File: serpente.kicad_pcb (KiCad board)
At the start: 2 copper layers, 24 x 22 mm, 31 parts, among them J1 USB_C_Receptacle_USB2.0, J2 Conn_Power, J3 Conn_GPIO, SW1 SW_RESET, U1 GD25Q32CNIGR, U2 MCP1700-3302E_SOT23, U3 ATSAMD21E18A

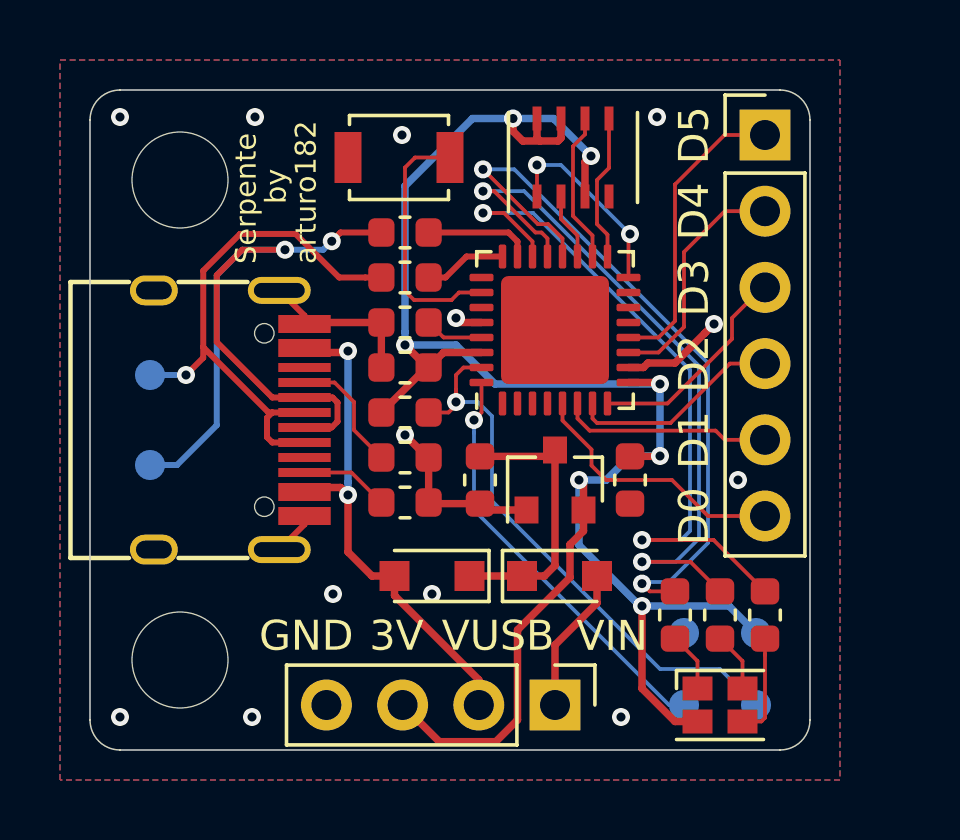
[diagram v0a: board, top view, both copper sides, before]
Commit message: Add Plug variant, make header positions same between variants
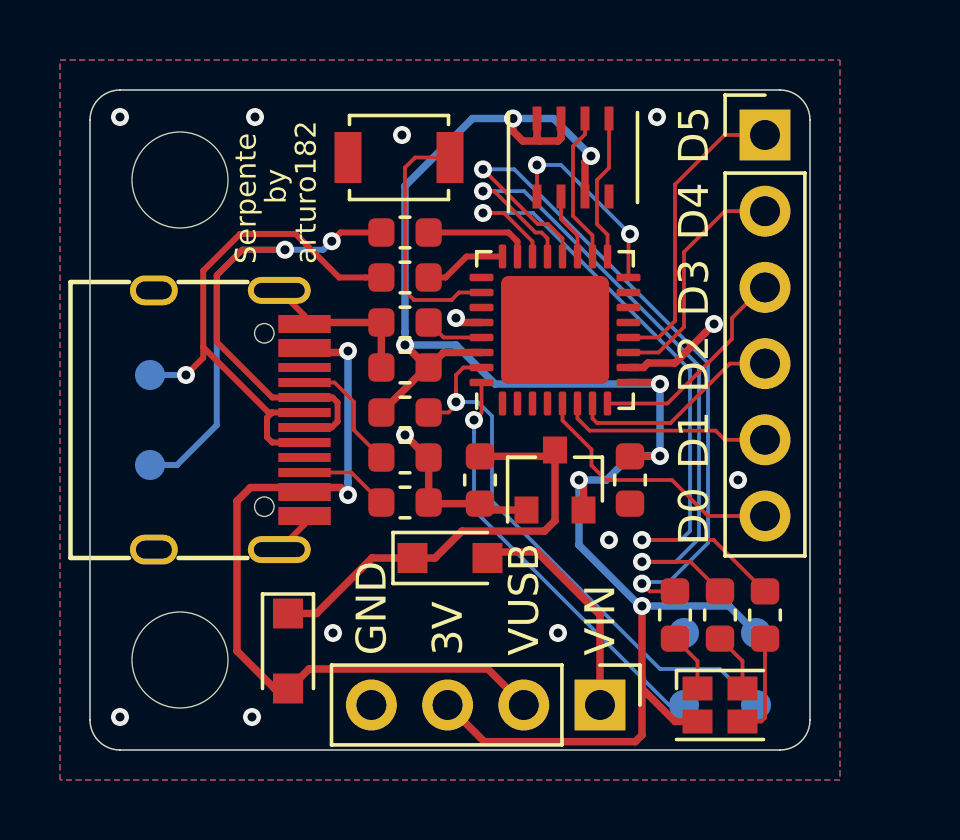
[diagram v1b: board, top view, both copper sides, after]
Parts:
- moved D1 5.41 mm to (123.6, 63.7), turned to 270 degrees
- moved D2 3.70 mm to (129.0, 60.6)
- moved J2 1.50 mm to (134.0, 65.5)
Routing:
- net VBUS: track 17.7 -> 26.7 mm
- net +5V: track 9.43 -> 15.1 mm
- net +3V3: track 67.8 -> 64.2 mm
- net VIN: track 4.88 -> 7.62 mm

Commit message: Fix GPIO numbers, add BOM, update README
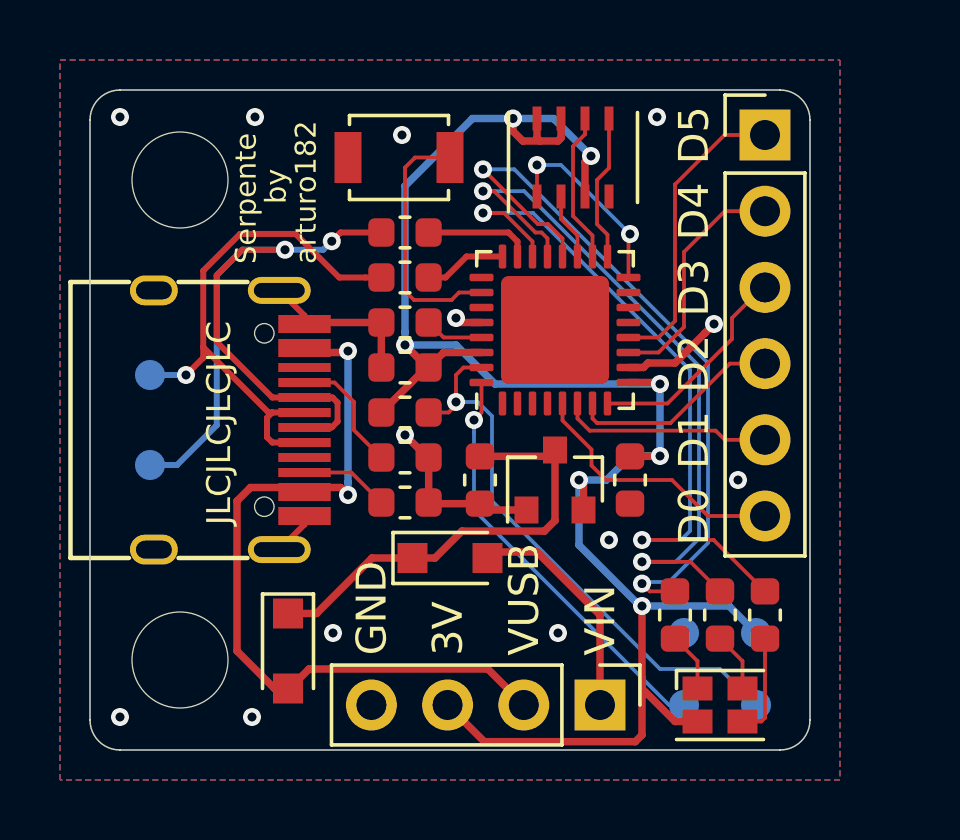
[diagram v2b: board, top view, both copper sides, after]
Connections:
- J3 pad 1: /GPIO0 -> /GPIO5
- J3 pad 2: /GPIO1 -> /GPIO4
- J3 pad 3: /GPIO2 -> /GPIO3
- J3 pad 4: /GPIO3 -> /GPIO2
- J3 pad 5: /GPIO4 -> /GPIO1
- J3 pad 6: /GPIO5 -> /GPIO0
- U3 pad 11: /GPIO1 -> /GPIO4
- U3 pad 12: /GPIO0 -> /GPIO5
- U3 pad 5: /GPIO5 -> /GPIO0
- U3 pad 6: /GPIO4 -> /GPIO1
- U3 pad 7: /GPIO3 -> /GPIO2
- U3 pad 8: /GPIO2 -> /GPIO3
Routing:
- net /GPIO5: track 8.95 -> 10.0 mm
- net /GPIO0: track 10.0 -> 8.95 mm
- net /GPIO4: track 7.04 -> 7.97 mm
- net /GPIO1: track 7.97 -> 7.04 mm
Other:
- board text added: "JLCJLCJLCJLC"
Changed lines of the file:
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@@
-(kicad_pcb (version 20171130) (host pcbnew 5.1.2)
+(kicad_pcb (version 20171130) (host pcbnew "(5.1.2)-2")
   (general
     (thickness 1.6)
-    (drawings 29)
+    (drawings 30)
     (tracks 307)
     (zones 0)
@@
     (pcbplotparams
       (layerselection 0x010fc_ffffffff)
-      (usegerberextensions false)
+      (usegerberextensions true)
       (usegerberattributes false)
       (usegerberadvancedattributes false)
@@
       (outputformat 1)
       (mirror false)
-      (drillshape 1)
+      (drillshape 0)
       (scaleselection 1)
-      (outputdirectory ""))
+      (outputdirectory "gerb/"))
   )
   (net 0 "")
@@
       (net 36 "Net-(U3-Pad13)"))
     (pad 12 smd roundrect (at -0.25 2.45 90) (size 0.25 0.8) (layers F.Cu F.Paste F.Mask) (roundrect_rratio 0.25)
-      (net 21 /GPIO0))
+      (net 16 /GPIO5))
     (pad 11 smd roundrect (at -0.75 2.45 90) (size 0.25 0.8) (layers F.Cu F.Paste F.Mask) (roundrect_rratio 0.25)
-      (net 20 /GPIO1))
+      (net 17 /GPIO4))
     (pad 10 smd roundrect (at -1.25 2.45 90) (size 0.25 0.8) (layers F.Cu F.Paste F.Mask) (roundrect_rratio 0.25)
       (net 2 GND))
@@
       (net 3 +3V3))
     (pad 8 smd roundrect (at -2.45 1.75 90) (size 0.8 0.25) (layers F.Cu F.Paste F.Mask) (roundrect_rratio 0.25)
+      (net 18 /GPIO3))
+    (pad 7 smd roundrect (at -2.45 1.25 90) (size 0.8 0.25) (layers F.Cu F.Paste F.Mask) (roundrect_rratio 0.25)
       (net 19 /GPIO2))
-    (pad 7 smd roundrect (at -2.45 1.25 90) (size 0.8 0.25) (layers F.Cu F.Paste F.Mask) (roundrect_rratio 0.25)
-      (net 18 /GPIO3))
     (pad 6 smd roundrect (at -2.45 0.75 90) (size 0.8 0.25) (layers F.Cu F.Paste F.Mask) (roundrect_rratio 0.25)
-      (net 17 /GPIO4))
+      (net 20 /GPIO1))
     (pad 5 smd roundrect (at -2.45 0.25 90) (size 0.8 0.25) (layers F.Cu F.Paste F.Mask) (roundrect_rratio 0.25)
-      (net 16 /GPIO5))
+      (net 21 /GPIO0))
     (pad 4 smd roundrect (at -2.45 -0.25 90) (size 0.8 0.25) (layers F.Cu F.Paste F.Mask) (roundrect_rratio 0.25)
       (net 37 "Net-(U3-Pad4)"))
@@
     (fp_line (start -0.635 -1.27) (end 1.27 -1.27) (layer F.Fab) (width 0.1))
     (pad 6 thru_hole oval (at 0 12.7) (size 1.7 1.7) (drill 1) (layers *.Cu *.Mask)
+      (net 21 /GPIO0))
+    (pad 5 thru_hole oval (at 0 10.16) (size 1.7 1.7) (drill 1) (layers *.Cu *.Mask)
+      (net 20 /GPIO1))
+    (pad 4 thru_hole oval (at 0 7.62) (size 1.7 1.7) (drill 1) (layers *.Cu *.Mask)
+      (net 19 /GPIO2))
+    (pad 3 thru_hole oval (at 0 5.08) (size 1.7 1.7) (drill 1) (layers *.Cu *.Mask)
+      (net 18 /GPIO3))
+    (pad 2 thru_hole oval (at 0 2.54) (size 1.7 1.7) (drill 1) (layers *.Cu *.Mask)
+      (net 17 /GPIO4))
+    (pad 1 thru_hole rect (at 0 0) (size 1.7 1.7) (drill 1) (layers *.Cu *.Mask)
       (net 16 /GPIO5))
-    (pad 5 thru_hole oval (at 0 10.16) (size 1.7 1.7) (drill 1) (layers *.Cu *.Mask)
-      (net 17 /GPIO4))
-    (pad 4 thru_hole oval (at 0 7.62) (size 1.7 1.7) (drill 1) (layers *.Cu *.Mask)
-      (net 18 /GPIO3))
-    (pad 3 thru_hole oval (at 0 5.08) (size 1.7 1.7) (drill 1) (layers *.Cu *.Mask)
-      (net 19 /GPIO2))
-    (pad 2 thru_hole oval (at 0 2.54) (size 1.7 1.7) (drill 1) (layers *.Cu *.Mask)
-      (net 20 /GPIO1))
-    (pad 1 thru_hole rect (at 0 0) (size 1.7 1.7) (drill 1) (layers *.Cu *.Mask)
-      (net 21 /GPIO0))
     (model ${KISYS3DMOD}/Connector_PinHeader_2.54mm.3dshapes/PinHeader_1x06_P2.54mm_Vertical.wrl
       (at (xyz 0 0 0))
@@
       (rotate (xyz 0 0 0))
     )
+  )
+  (gr_text JLCJLCJLCJLC (at 121.3 56.1 90) (layer F.SilkS)
+    (effects (font (size 0.8 0.8) (thickness 0.15)))
   )
   (gr_text 3V (at 128.9304 63.8556 90) (layer F.SilkS)
@@
   (segment (start 130.25 60.4) (end 131.9 60.4) (width 0.25) (layer F.Cu) (net 15))
   (segment (start 131.9 60.4) (end 134 62.5) (width 0.25) (layer F.Cu) (net 15))
-  (segment (start 137.6 59.2) (end 136.4 58) (width 0.127) (layer F.Cu) (net 16))
-  (segment (start 136.4 58) (end 134.2 58) (width 0.127) (layer F.Cu) (net 16))
-  (segment (start 132.75 56.016284) (end 132.75 55.45) (width 0.127) (layer F.Cu) (net 16))
-  (segment (start 134.2 58) (end 133.716858 57.516858) (width 0.127) (layer F.Cu) (net 16))
-  (segment (start 139.5 59.2) (end 137.6 59.2) (width 0.127) (layer F.Cu) (net 16))
-  (segment (start 133.716858 57.516858) (end 133.716858 56.983142) (width 0.127) (layer F.Cu) (net 16))
-  (segment (start 133.716858 56.983142) (end 132.75 56.016284) (width 0.127) (layer F.Cu) (net 16))
-  (segment (start 138.16 56.66) (end 139.5 56.66) (width 0.127) (layer F.Cu) (net 17))
-  (segment (start 137.85401 56.35401) (end 138.16 56.66) (width 0.127) (layer F.Cu) (net 17))
-  (segment (start 133.65401 56.35401) (end 137.85401 56.35401) (width 0.127) (layer F.Cu) (net 17))
-  (segment (start 133.25 55.45) (end 133.25 55.95) (width 0.127) (layer F.Cu) (net 17))
-  (segment (start 133.25 55.95) (end 133.65401 56.35401) (width 0.127) (layer F.Cu) (net 17))
-  (segment (start 138.33 54.12) (end 139.5 54.12) (width 0.127) (layer F.Cu) (net 18))
-  (segment (start 136.35 56.1) (end 138.33 54.12) (width 0.127) (layer F.Cu) (net 18))
-  (segment (start 133.9 56.1) (end 136.35 56.1) (width 0.127) (layer F.Cu) (net 18))
-  (segment (start 133.75 55.45) (end 133.75 55.95) (width 0.127) (layer F.Cu) (net 18))
-  (segment (start 133.75 55.95) (end 133.9 56.1) (width 0.127) (layer F.Cu) (net 18))
-  (segment (start 139.42 51.58) (end 139.5 51.58) (width 0.127) (layer F.Cu) (net 19))
-  (segment (start 138.4 52.6) (end 139.42 51.58) (width 0.127) (layer F.Cu) (net 19))
-  (segment (start 138.4 53.3) (end 138.4 52.6) (width 0.127) (layer F.Cu) (net 19))
-  (segment (start 134.25 55.45) (end 136.25 55.45) (width 0.127) (layer F.Cu) (net 19))
-  (segment (start 136.25 55.45) (end 138.4 53.3) (width 0.127) (layer F.Cu) (net 19))
-  (segment (start 138.16 49.04) (end 139.5 49.04) (width 0.127) (layer F.Cu) (net 20))
-  (segment (start 136.8 50.4) (end 138.16 49.04) (width 0.127) (layer F.Cu) (net 20))
-  (segment (start 136.8 52.9) (end 136.8 50.4) (width 0.127) (layer F.Cu) (net 20))
-  (segment (start 134.95 53.75) (end 135.95 53.75) (width 0.127) (layer F.Cu) (net 20))
-  (segment (start 135.95 53.75) (end 136.8 52.9) (width 0.127) (layer F.Cu) (net 20))
-  (segment (start 138.15 46.5) (end 139.5 46.5) (width 0.127) (layer F.Cu) (net 21))
-  (segment (start 136.5 48.15) (end 138.15 46.5) (width 0.127) (layer F.Cu) (net 21))
-  (segment (start 136.5 52.7) (end 136.5 48.15) (width 0.127) (layer F.Cu) (net 21))
-  (segment (start 134.95 53.25) (end 135.95 53.25) (width 0.127) (layer F.Cu) (net 21))
-  (segment (start 135.95 53.25) (end 136.5 52.7) (width 0.127) (layer F.Cu) (net 21))
+  (segment (start 137.6 59.2) (end 136.4 58) (width 0.127) (layer F.Cu) (net 21))
+  (segment (start 136.4 58) (end 134.2 58) (width 0.127) (layer F.Cu) (net 21))
+  (segment (start 132.75 56.016284) (end 132.75 55.45) (width 0.127) (layer F.Cu) (net 21))
+  (segment (start 134.2 58) (end 133.716858 57.516858) (width 0.127) (layer F.Cu) (net 21))
+  (segment (start 139.5 59.2) (end 137.6 59.2) (width 0.127) (layer F.Cu) (net 21))
+  (segment (start 133.716858 57.516858) (end 133.716858 56.983142) (width 0.127) (layer F.Cu) (net 21))
+  (segment (start 133.716858 56.983142) (end 132.75 56.016284) (width 0.127) (layer F.Cu) (net 21))
+  (segment (start 138.16 56.66) (end 139.5 56.66) (width 0.127) (layer F.Cu) (net 20))
+  (segment (start 137.85401 56.35401) (end 138.16 56.66) (width 0.127) (layer F.Cu) (net 20))
+  (segment (start 133.65401 56.35401) (end 137.85401 56.35401) (width 0.127) (layer F.Cu) (net 20))
+  (segment (start 133.25 55.45) (end 133.25 55.95) (width 0.127) (layer F.Cu) (net 20))
+  (segment (start 133.25 55.95) (end 133.65401 56.35401) (width 0.127) (layer F.Cu) (net 20))
+  (segment (start 138.33 54.12) (end 139.5 54.12) (width 0.127) (layer F.Cu) (net 19))
+  (segment (start 136.35 56.1) (end 138.33 54.12) (width 0.127) (layer F.Cu) (net 19))
+  (segment (start 133.9 56.1) (end 136.35 56.1) (width 0.127) (layer F.Cu) (net 19))
+  (segment (start 133.75 55.45) (end 133.75 55.95) (width 0.127) (layer F.Cu) (net 19))
+  (segment (start 133.75 55.95) (end 133.9 56.1) (width 0.127) (layer F.Cu) (net 19))
+  (segment (start 139.42 51.58) (end 139.5 51.58) (width 0.127) (layer F.Cu) (net 18))
+  (segment (start 138.4 52.6) (end 139.42 51.58) (width 0.127) (layer F.Cu) (net 18))
+  (segment (start 138.4 53.3) (end 138.4 52.6) (width 0.127) (layer F.Cu) (net 18))
+  (segment (start 134.25 55.45) (end 136.25 55.45) (width 0.127) (layer F.Cu) (net 18))
+  (segment (start 136.25 55.45) (end 138.4 53.3) (width 0.127) (layer F.Cu) (net 18))
+  (segment (start 138.16 49.04) (end 139.5 49.04) (width 0.127) (layer F.Cu) (net 17))
+  (segment (start 136.8 50.4) (end 138.16 49.04) (width 0.127) (layer F.Cu) (net 17))
+  (segment (start 136.8 52.9) (end 136.8 50.4) (width 0.127) (layer F.Cu) (net 17))
+  (segment (start 134.95 53.75) (end 135.95 53.75) (width 0.127) (layer F.Cu) (net 17))
+  (segment (start 135.95 53.75) (end 136.8 52.9) (width 0.127) (layer F.Cu) (net 17))
+  (segment (start 138.15 46.5) (end 139.5 46.5) (width 0.127) (layer F.Cu) (net 16))
+  (segment (start 136.5 48.15) (end 138.15 46.5) (width 0.127) (layer F.Cu) (net 16))
+  (segment (start 136.5 52.7) (end 136.5 48.15) (width 0.127) (layer F.Cu) (net 16))
+  (segment (start 134.95 53.25) (end 135.95 53.25) (width 0.127) (layer F.Cu) (net 16))
+  (segment (start 135.95 53.25) (end 136.5 52.7) (width 0.127) (layer F.Cu) (net 16))
   (via (at 130.1 47.645994) (size 0.6) (drill 0.3) (layers F.Cu B.Cu) (net 22))
   (segment (start 130.105218 47.645994) (end 130.1 47.645994) (width 0.127) (layer F.Cu) (net 22))

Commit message: Final rev 2 release!
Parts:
- removed R7, R8: 22R, Resistor_SMD:R_0603_1608Metric
- added TP7: TP_RESET, TestPoint:TestPoint_Pad_D1.0mm, B.Cu at (123.2, 47.0)
- D3: value LED_ARGB -> LED_RBAG
- J2: footprint Connector_PinHeader_2.54mm:PinHeader_1x04_P2.54mm_Vertical -> Connector_PinHeader_2.54mm_Extra:PinHeader_1x04_P2.54mm_Vertical_Castellated
- J3: footprint Connector_PinHeader_2.54mm:PinHeader_1x06_P2.54mm_Vertical -> Connector_PinHeader_2.54mm_Extra:PinHeader_1x06_P2.54mm_Vertical_Castellated
- SW1: footprint Button_Switch_SMD:SW_SPST_B3U-1000P -> Button_Switch_SMD:SW_SPST_B3U-1000P-B
- moved D1 6.70 mm to (128.0, 58.6), turned to 0 degrees
- moved C2 3.30 mm to (127.5, 51.0)
- moved C1 3.24 mm to (131.8, 60.7), turned to 0 degrees
- moved R3 2.50 mm to (140.5, 62.4)
- moved R4 1.80 mm to (127.5, 55.5)
- moved R5 1.80 mm to (127.5, 57.0)
- moved R6 1.80 mm to (127.5, 54.0)
- moved J2 1.23 mm to (134.1, 64.3)
- moved D2 1.00 mm to (128.0, 60.5)
- moved R1 1.00 mm to (137.5, 62.4)
- moved D3 1.00 mm to (139.0, 65.4)
- moved C3 0.63 mm to (134.4, 58.2), turned to 90 degrees
- moved U2 0.63 mm to (131.9, 58.2)
- moved TP3 0.56 mm to (139.8, 63.0)
- moved TP1 0.55 mm to (139.8, 65.5)
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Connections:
- net Net-(SW1-Pad2) renamed /~RESET~
- D3 pad 3: Net-(D3-Pad3) -> +3V3
- D3 pad 4: +3V3 -> Net-(D3-Pad4)
- J2 pad 3: +3V3 -> GND
- J2 pad 4: GND -> +3V3
- R2 pad 1: Net-(D3-Pad3) -> Net-(D3-Pad4)
- U3 pad 20: /LED_R -> /LED_G
- U3 pad 21: /LED_B -> /LED_R
- U3 pad 22: /LED_G -> /LED_B
- U3 pad 23: Net-(R7-Pad1) -> /USB_D-
- U3 pad 24: Net-(R8-Pad1) -> /USB_D+
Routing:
- net GND: track 17.8 -> 23.1 mm, vias 13 -> 11
- net /USB_D-: track 25.4 -> 30.6 mm
- net VBUS: track 26.7 -> 22.3 mm, vias 2 -> 3
- net /USB_D+: track 18.5 -> 22.5 mm
- net +5V: track 15.1 -> 11.3 mm
- net /~RESET~: track 8.53 -> 12.3 mm, vias 0 -> 3
- net /LED_G: track 23.5 -> 27.1 mm
- net Net-(R7-Pad1): track 3.59 -> 0.00 mm
- net Net-(D3-Pad3): track 3.44 -> 0.00 mm
- net /GPIO4: track 7.97 -> 10.8 mm
- net Net-(D3-Pad4): track 0.00 -> 2.87 mm
- net /GPIO3: track 7.26 -> 10.1 mm
- net Net-(R8-Pad1): track 2.75 -> 0.00 mm
- net VIN: track 7.62 -> 9.98 mm
- net /GPIO5: track 10.0 -> 12.3 mm
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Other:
- board size 24 x 22 mm -> 24.8 x 22 mm
- board text added: "CLK"
- board text added: "DAT"
- board text added: "IN"
- board text added: "R2"
- board text added: "RST"
- board text added: "USB"
- board text added: "V"
- board text removed: "C"
- board text removed: "G"
- board text removed: "JLCJLCJLCJLC"
- board text removed: "VIN"
- board text removed: "VUSB"
